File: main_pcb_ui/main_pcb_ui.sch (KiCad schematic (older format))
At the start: 11 parts, among them J1 Conn_02x02_Odd_Even, J2 Conn_02x02_Odd_Even, J3 Conn_02x02_Odd_Even, J4 Conn_02x02_Odd_Even, SW1 SP+, SW2 SP-, SW3 TRIG, SW4 BR+, SW5 BR-

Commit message: Routed and updated UI board
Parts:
- added R2, R3, R4, R5, R6: 1k, Resistor_SMD:R_0603_1608Metric, symbol Device:R
- J1, J2, J3, J4: footprint Connector_PinHeader_2.54mm:PinHeader_2x02_P2.54mm_Vertical -> Connector_PinSocket_2.54mm:PinSocket_2x02_P2.54mm_Vertical
- SW1, SW2, SW3, SW4, SW5: symbol Switch:SW_MEC_5E -> Switch:SW_SPST
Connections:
- net BR+: now also R5.2; no longer SW4.2
- net BR-: now also J4.1 (Pin_1), R6.2; no longer J3.3 (Pin_3), SW5.2
- net GND: now also J2.4 (Pin_4), SW1.2 (B), SW2.2 (B), SW3.2 (B), SW4.2 (B), SW5.2 (B); no longer J1.4 (Pin_4), J2.1 (Pin_1), SW1.3 (K), SW1.4 (A), SW2.3 (K), SW2.4 (A), SW3.3 (K), SW3.4 (A), SW4.3 (K), SW4.4 (A), SW5.3 (K), SW5.4 (A)
- net LED: now also J3.3 (Pin_3); no longer J4.1 (Pin_1)
- net SP+: now also R2.2; no longer SW1.2
- net SP-: now also J1.2 (Pin_2), R3.2; no longer J2.4 (Pin_4), SW2.2
- net TRIG: now also J1.4 (Pin_4), R4.2; no longer J1.2 (Pin_2), SW3.2
- new net +3V3: J2.1 (Pin_1), R2.1, R3.1, R4.1, R5.1, R6.1

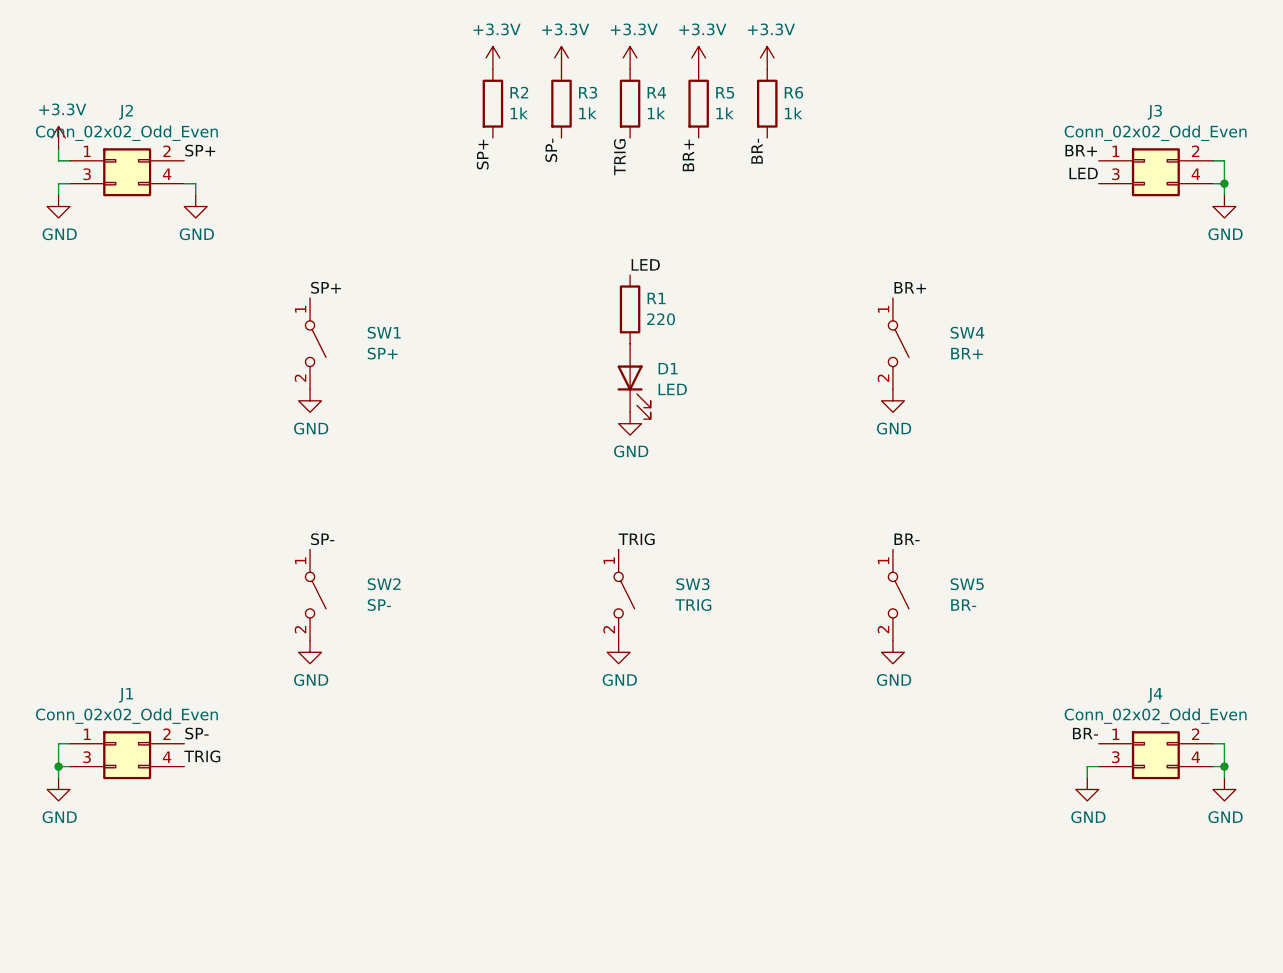
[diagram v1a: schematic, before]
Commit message: Added power button to ui, increased size of board, and moved connectors 15 mm up
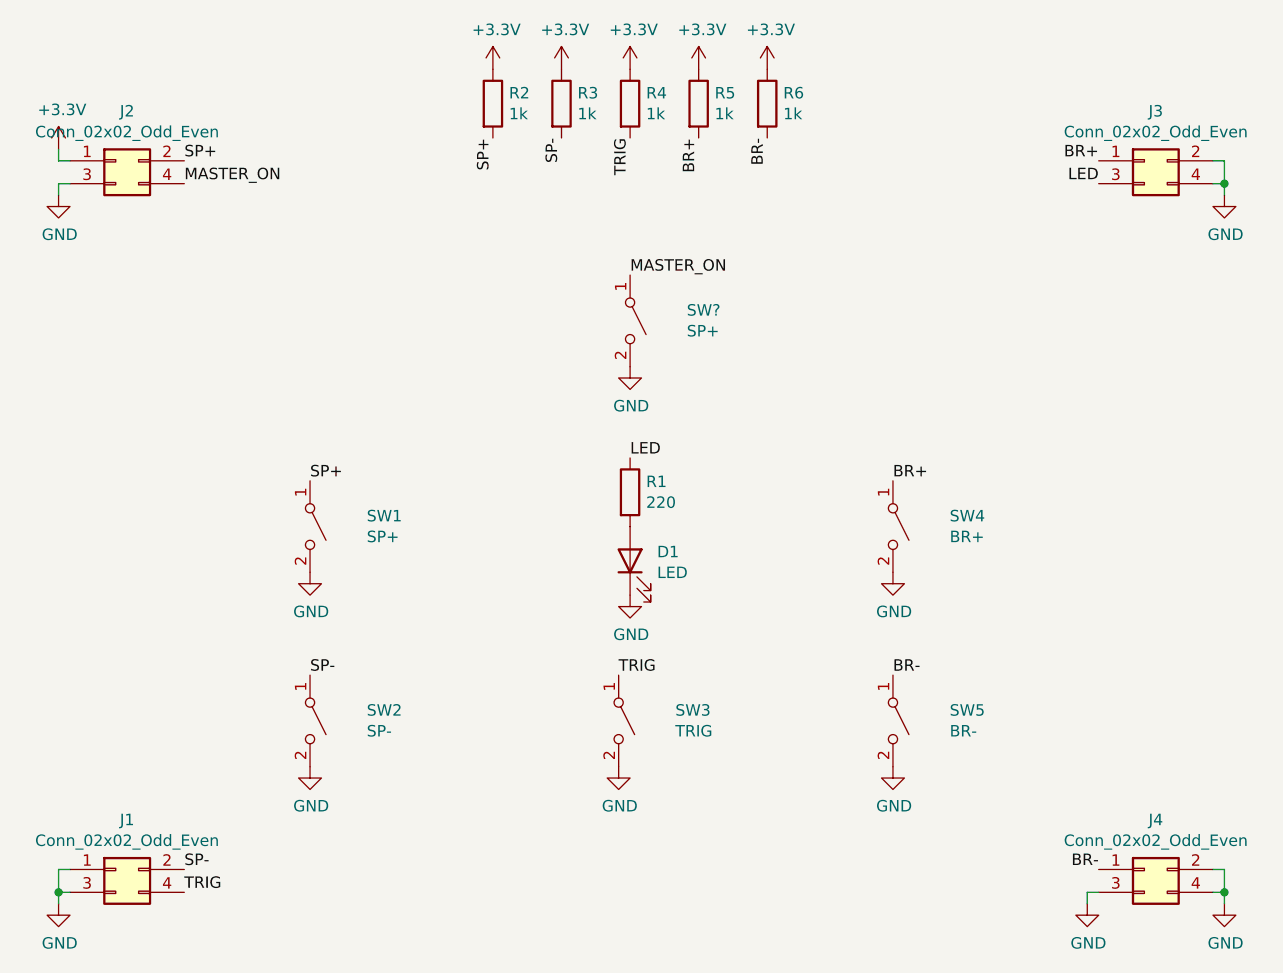
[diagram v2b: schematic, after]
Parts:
- added SW?: SP+, Button_Switch_THT:SW_PUSH_6mm_H8mm, symbol Switch:SW_SPST
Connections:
- net GND: now also SW?.2 (B); no longer J2.4 (Pin_4)
- new net MASTER_ON: J2.4 (Pin_4), SW?.1 (A)
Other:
- moved on the sheet: D1, J1, J4, R1, SW1, SW2, SW3, SW4, SW5

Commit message: Generated output files for main_pcb_ui
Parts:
- gave numbers to parts that had none: 1
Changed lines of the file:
@@
 $EndComp
 $Comp
-L power:GND #PWR?
+L power:GND #PWR0109
 U 1 1 617DE099
 P 5300 2800
-F 0 "#PWR?" H 5300 2550 50  0001 C CNN
+F 0 "#PWR0109" H 5300 2550 50  0001 C CNN
 F 1 "GND" H 5305 2627 50  0000 C CNN
 F 2 "" H 5300 2800 50  0001 C CNN
@@
 $EndComp
 $Comp
-L Switch:SW_SPST SW?
+L Switch:SW_SPST SW6
 U 1 1 617DE0A2
 P 5300 2600
-F 0 "SW?" V 5254 2848 50  0000 L CNN
+F 0 "SW6" V 5254 2848 50  0000 L CNN
 F 1 "SP+" V 5345 2848 50  0000 L CNN
 F 2 "Button_Switch_THT:SW_PUSH_6mm_H8mm" H 5300 2900 50  0001 C CNN

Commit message: Fixed wrong part number
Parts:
- J2: MPN C66690 -> DS1023-2*2SF11; Manufacturer BOOMELE -> CONNFLY Elec
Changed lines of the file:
@@
 F 2 "Connector_PinSocket_2.54mm:PinSocket_2x02_P2.54mm_Vertical" H 3050 1900 50  0001 C CNN
 F 3 "~" H 3050 1900 50  0001 C CNN
-F 4 "C66690" H 3050 1900 50  0001 C CNN "MPN"
-F 5 "BOOMELE" H 3050 1900 50  0001 C CNN "Manufacturer"
+F 4 "DS1023-2*2SF11" H 3050 1900 50  0001 C CNN "MPN"
+F 5 "CONNFLY Elec" H 3050 1900 50  0001 C CNN "Manufacturer"
 	1    3050 1900
 	1    0    0    -1
